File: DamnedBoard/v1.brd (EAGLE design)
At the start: 50.8 x 16.5 mm, 19 parts, among them J1 CORTEX_DEBUG_SMD, U1 EFM32ZG108, U2 MAX44009EDT+T21-0490D-M

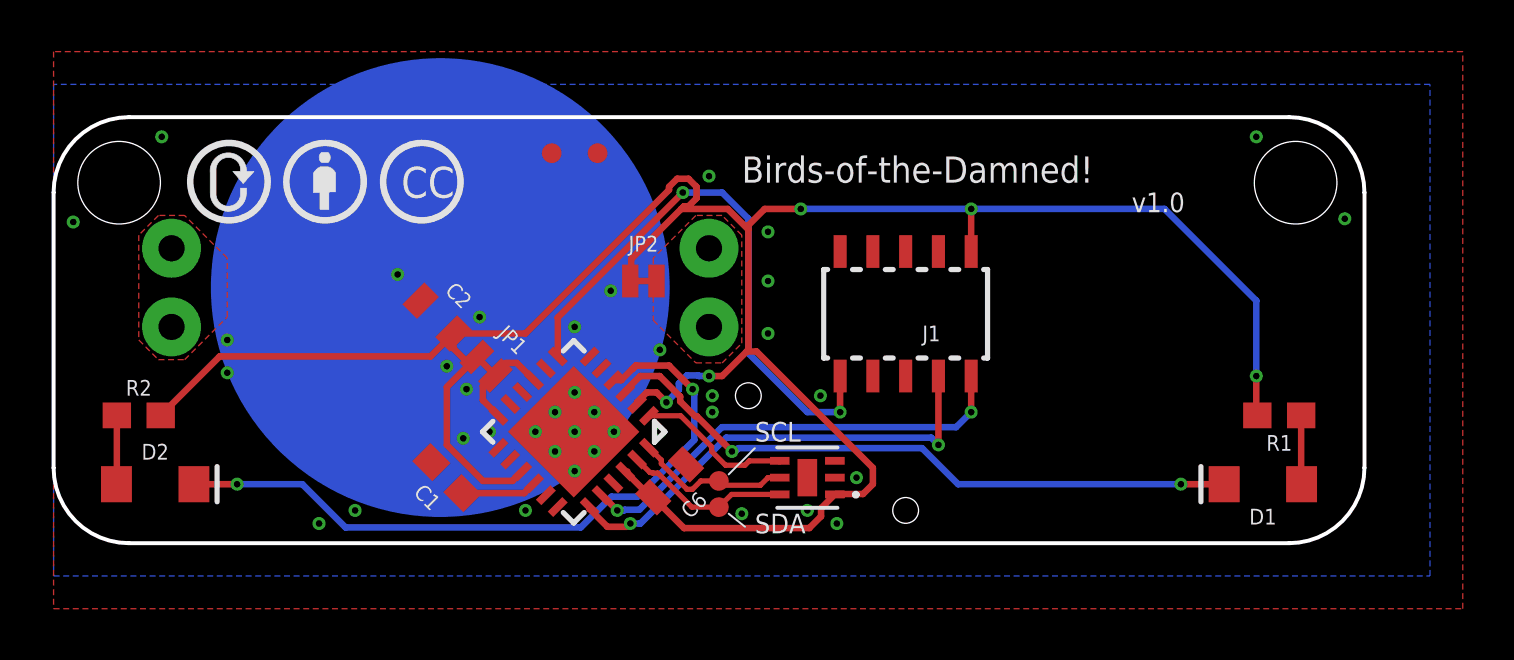
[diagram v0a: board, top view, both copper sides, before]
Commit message: Added pullups to i2c
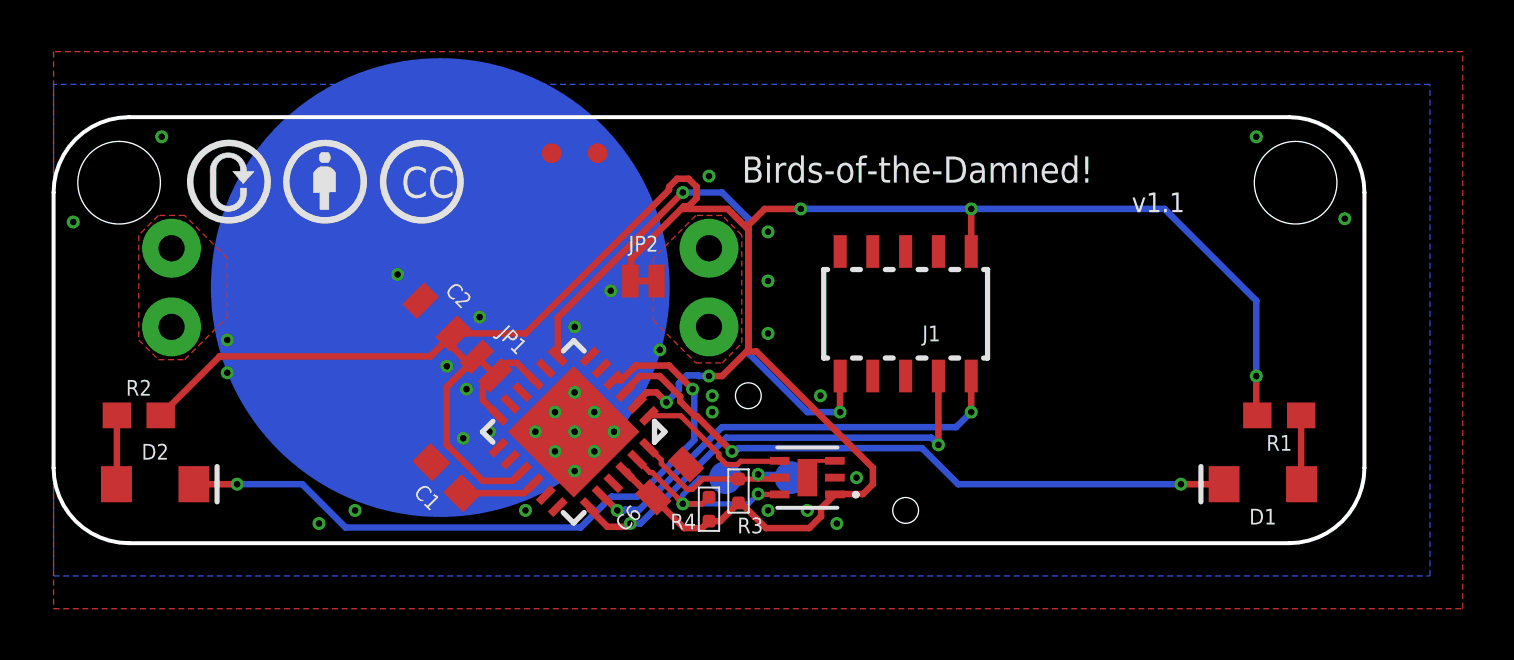
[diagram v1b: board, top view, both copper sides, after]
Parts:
- added R3, R4: 1K, Seeed-Resistor:R0402
- TP1, TP2: value TEST-POINT3 -> TEST-POINT3X5; device SparkFun-Connectors:PAD.03X.03 -> SparkFun-Connectors:PAD.03X.05
- moved TP2 2.80 mm to (28.6, 2.54), flipped to the bottom
- moved TP1 1.17 mm to (26.0, 2.54), flipped to the bottom
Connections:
- net SCL: now also R4.2
- net SDA: now also R3.1
- net VCC: now also R3.2, R4.1
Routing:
- net SDA: track 6.52 -> 9.84 mm, vias 0 -> 2
- net VSS: track 0.00 -> 1.63 mm
- net SCL: track 6.32 -> 7.51 mm, vias 0 -> 1
- net VCC: track 98.8 -> 99.6 mm
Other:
- board text added: "v1.1"
- board text removed: "v1.0"

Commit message: V1.1 pinout with all tests points.
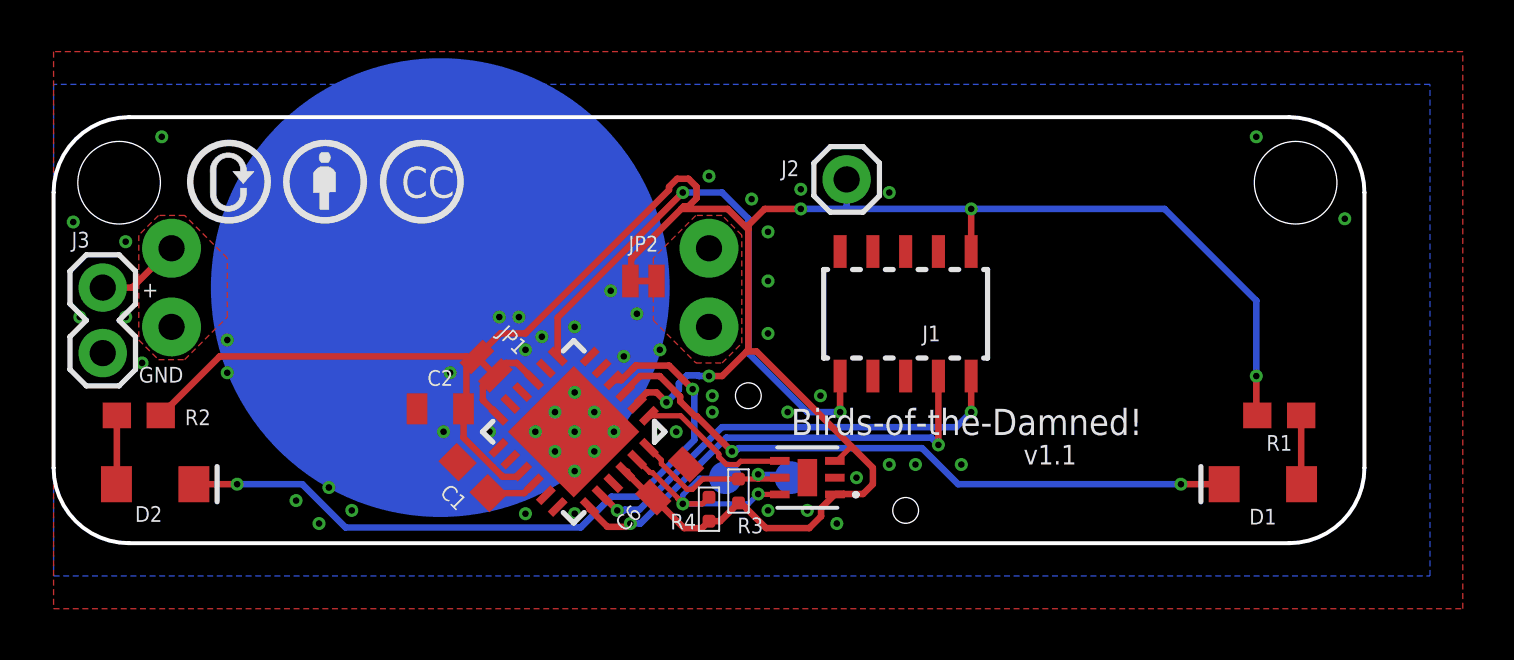
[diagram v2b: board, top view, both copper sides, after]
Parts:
- removed TP3, TP4: TEST-POINT3, SparkFun-Connectors:PAD.03X.03
- added J2: I_TEST, SparkFun-Connectors:1X01
- added J3: TEST, SparkFun-Connectors:1X02
- moved C2 3.56 mm to (15.0, 5.21), turned to 0 degrees
- moved C1 1.02 mm to (16.3, 2.54)
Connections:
- net +R: now also J3.2
- net VCC: now also J2.1, U2.3
- net VSS: now also J3.1; no longer TP3.P$1, TP4.P$1, U2.3
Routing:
- net +R: track 0.00 -> 3.30 mm
- net DCP: track 2.94 -> 1.92 mm
- net VSS: track 1.63 -> 0.71 mm, vias 39 -> 57
- net VCC: track 99.6 -> 98.9 mm
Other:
- board text added: "+"
- board text added: "GND"

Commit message: Progress on the adjustable version.
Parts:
- removed JP1: JUMPER-SMT_2_NC_TRACE_NO-SILK, SparkFun-Jumpers:SMT-JUMPER_2_NC_TRACE_NO-SILK
- added C3: 10nf, Seeed-Capacitor:C0402
- added R5: PV36W104C01B00, boneyard:POT_PV36W
- moved C2 2.47 mm to (16.4, 7.24), turned to 315 degrees
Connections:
- removed net AVDD: JP1.2, U1.12, U1.9
- removed net PA0: U1.1, U2.4
- removed net PC0: D1.C, U1.3
- removed net PC1: D2.C, U1.4
- new net ADJ: R5.2, U1.4
- new net EYE_L: D1.C, U1.1
- new net EYE_R: D2.C, U1.3
- new net WAKE: U1.21, U2.4
- net VCC: now also C3.2, R5.3, U1.12, U1.9; no longer JP1.1
- net VSS: now also C3.1, R5.1
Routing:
- net PC1: track 27.3 -> 0.00 mm, vias 2 -> 0
- net PC0: track 25.4 -> 0.00 mm, vias 2 -> 0
- net EYE_R: track 0.00 -> 23.5 mm, vias 0 -> 2
- net EYE_L: track 0.00 -> 19.7 mm, vias 0 -> 2
- net VCC: track 98.9 -> 85.7 mm, vias 5 -> 4
- net PA0: track 6.10 -> 0.00 mm
- net AVDD: track 4.09 -> 0.00 mm
- net VSS: vias 57 -> 51

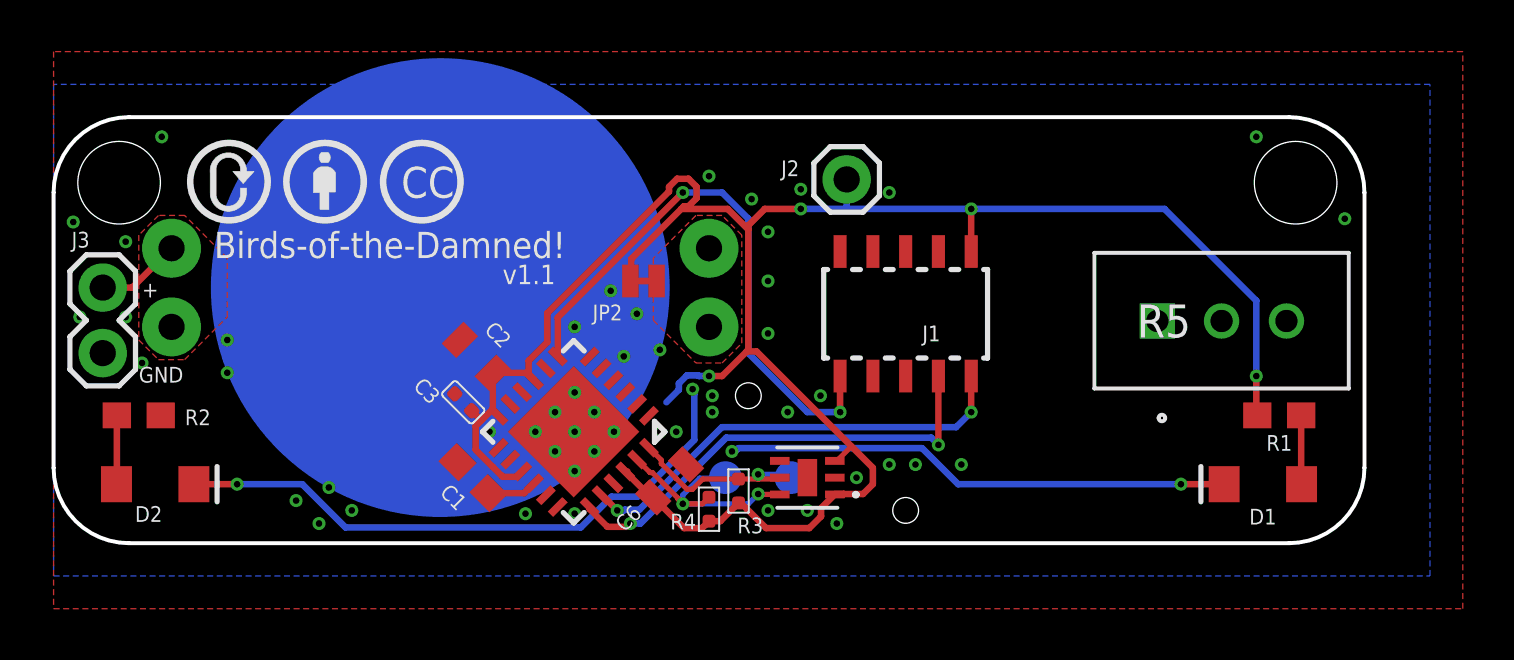
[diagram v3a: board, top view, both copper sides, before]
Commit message: Progress on v1.1
Added trim pot to use for light threshold adjustment.
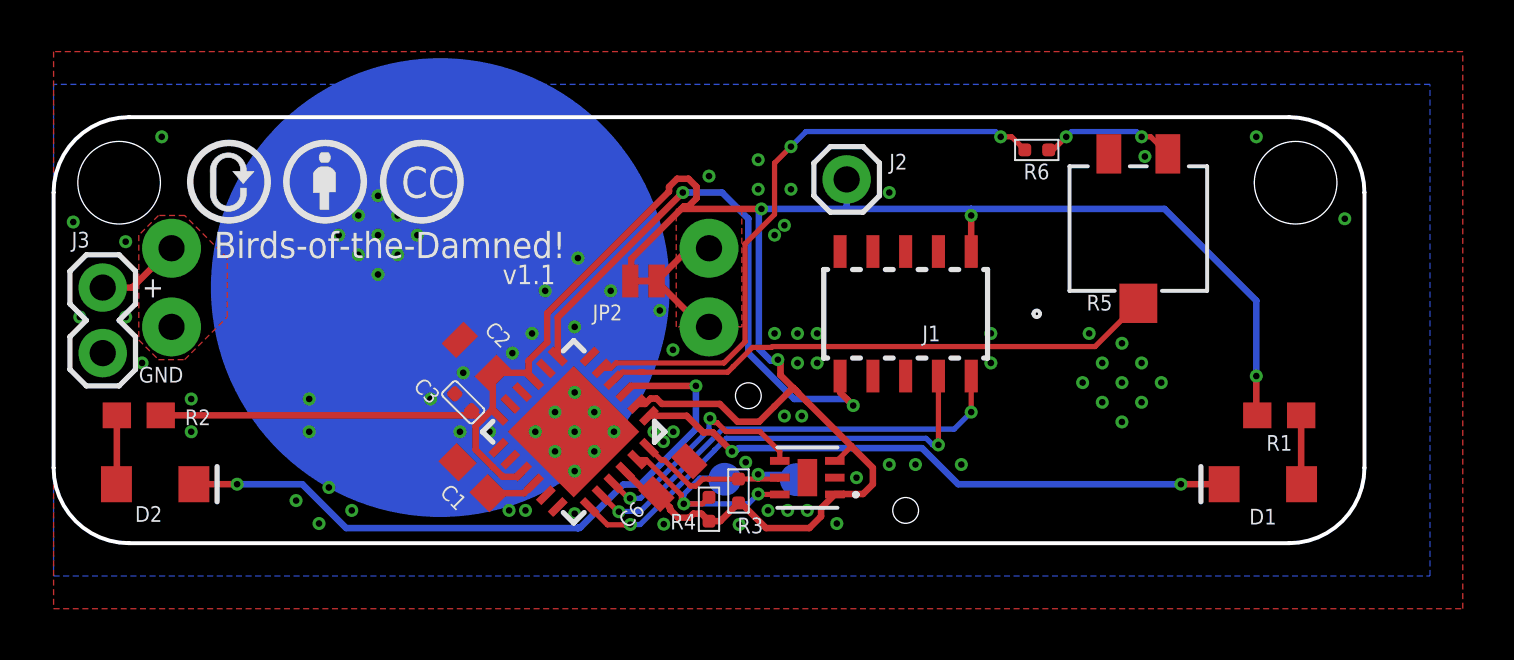
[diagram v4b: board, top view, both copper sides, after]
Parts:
- added R6: 1K, Seeed-Resistor:R0402
- R5: value PV36W104C01B00 -> 23BR100KLFTR; device boneyard:POT_PV36W -> boneyard:SOT_23BR100KLFTR
- moved R5 6.73 mm to (42.0, 12.2)
- moved TP2 0.22 mm to (28.8, 2.46)
- moved C6 0.18 mm to (24.0, 2.54)
- moved TP1 0.07 mm to (26.0, 2.48)
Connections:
- new net ADJ_PWR: R6.1, U1.5
- new net ADJ_PWR_SAFE: R5.3, R6.2
- net VCC: no longer R5.3
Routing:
- net ADJ_PWR: track 0.00 -> 23.9 mm, vias 0 -> 2
- net ADJ: track 0.00 -> 21.7 mm
- net VCC: track 85.7 -> 101.1 mm
- net WAKE: track 0.00 -> 9.10 mm, vias 0 -> 2
- net +L: track 0.00 -> 5.33 mm
- net ADJ_PWR_SAFE: track 0.00 -> 5.27 mm, vias 0 -> 2
- net EYE_L: track 19.7 -> 23.5 mm
- net EYE_R: track 23.5 -> 26.3 mm
- net VSS: vias 51 -> 90

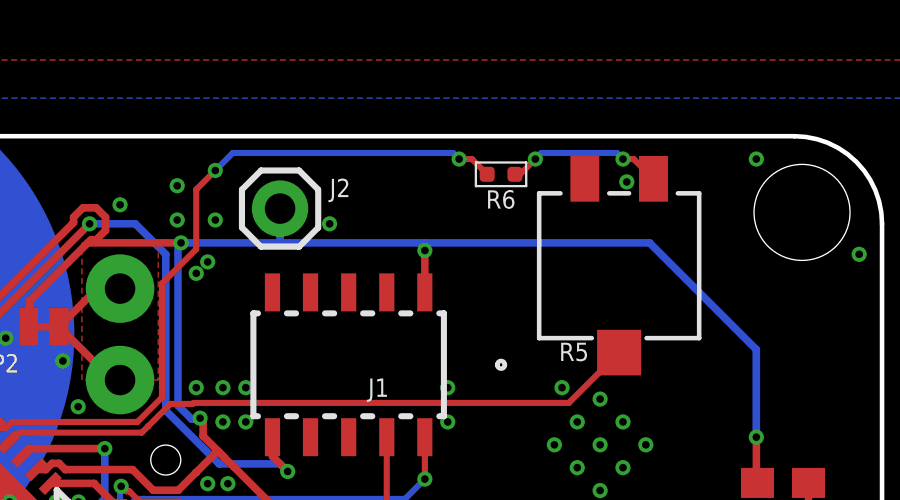
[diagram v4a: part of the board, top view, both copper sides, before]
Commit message: Adding Yakindu machine for firmware.
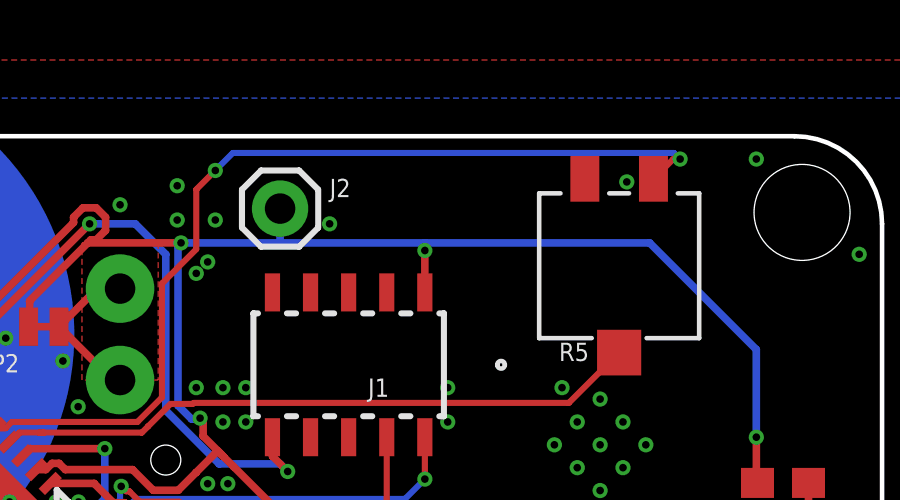
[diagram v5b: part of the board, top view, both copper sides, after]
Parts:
- removed R6: 1K, Seeed-Resistor:R0402
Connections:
- removed net ADJ_PWR_SAFE: R5.3, R6.2
- net ADJ_PWR: now also R5.3; no longer R6.1
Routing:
- net ADJ_PWR: track 23.9 -> 31.3 mm
- net ADJ_PWR_SAFE: track 5.27 -> 0.00 mm, vias 2 -> 0
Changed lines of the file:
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@@
 <layers>
 <layer number="1" name="Top" color="4" fill="1" visible="yes" active="yes"/>
-<layer number="16" name="Bottom" color="1" fill="1" visible="no" active="yes"/>
+<layer number="16" name="Bottom" color="1" fill="1" visible="yes" active="yes"/>
 <layer number="17" name="Pads" color="2" fill="1" visible="yes" active="yes"/>
 <layer number="18" name="Vias" color="2" fill="1" visible="yes" active="yes"/>
 <layer number="19" name="Unrouted" color="6" fill="1" visible="yes" active="yes"/>
 <layer number="20" name="Dimension" color="24" fill="1" visible="yes" active="yes"/>
-<layer number="21" name="tPlace" color="7" fill="1" visible="yes" active="yes"/>
-<layer number="22" name="bPlace" color="7" fill="1" visible="no" active="yes"/>
-<layer number="23" name="tOrigins" color="15" fill="1" visible="yes" active="yes"/>
-<layer number="24" name="bOrigins" color="15" fill="1" visible="no" active="yes"/>
-<layer number="25" name="tNames" color="7" fill="1" visible="yes" active="yes"/>
-<layer number="26" name="bNames" color="7" fill="1" visible="no" active="yes"/>
+<layer number="21" name="tPlace" color="7" fill="1" visible="no" active="yes"/>
+<layer number="22" name="bPlace" color="7" fill="1" visible="yes" active="yes"/>
+<layer number="23" name="tOrigins" color="15" fill="1" visible="no" active="yes"/>
+<layer number="24" name="bOrigins" color="15" fill="1" visible="yes" active="yes"/>
+<layer number="25" name="tNames" color="7" fill="1" visible="no" active="yes"/>
+<layer number="26" name="bNames" color="7" fill="1" visible="yes" active="yes"/>
 <layer number="27" name="tValues" color="7" fill="1" visible="no" active="yes"/>
 <layer number="28" name="bValues" color="7" fill="1" visible="no" active="yes"/>
@@
 <layer number="37" name="tTest" color="7" fill="1" visible="no" active="yes"/>
 <layer number="38" name="bTest" color="7" fill="1" visible="no" active="yes"/>
-<layer number="39" name="tKeepout" color="4" fill="11" visible="yes" active="yes"/>
-<layer number="40" name="bKeepout" color="1" fill="11" visible="no" active="yes"/>
-<layer number="41" name="tRestrict" color="4" fill="10" visible="yes" active="yes"/>
-<layer number="42" name="bRestrict" color="1" fill="10" visible="no" active="yes"/>
+<layer number="39" name="tKeepout" color="4" fill="11" visible="no" active="yes"/>
+<layer number="40" name="bKeepout" color="1" fill="11" visible="yes" active="yes"/>
+<layer number="41" name="tRestrict" color="4" fill="10" visible="no" active="yes"/>
+<layer number="42" name="bRestrict" color="1" fill="10" visible="yes" active="yes"/>
 <layer number="43" name="vRestrict" color="2" fill="10" visible="no" active="yes"/>
 <layer number="44" name="Drills" color="7" fill="1" visible="no" active="yes"/>
@@
 <layer number="49" name="Reference" color="7" fill="1" visible="no" active="yes"/>
 <layer number="50" name="dxf" color="7" fill="1" visible="no" active="no"/>
-<layer number="51" name="tDocu" color="7" fill="1" visible="yes" active="yes"/>
-<layer number="52" name="bDocu" color="7" fill="1" visible="no" active="yes"/>
+<layer number="51" name="tDocu" color="7" fill="1" visible="no" active="yes"/>
+<layer number="52" name="bDocu" color="7" fill="1" visible="yes" active="yes"/>
 <layer number="53" name="tGND_GNDA" color="7" fill="9" visible="no" active="no"/>
 <layer number="54" name="bGND_GNDA" color="1" fill="9" visible="no" active="no"/>
@@
 <attribute name="VALUE" x="13.809540625" y="5.371196875" size="0.635" layer="27" font="vector" ratio="10" rot="R315"/>
 </element>
-<element name="R6" library="Seeed-Resistor" library_urn="urn:adsk.eagle:library:474" package="R0402" package3d_urn="urn:adsk.eagle:package:32792/1" value="1K" x="38.1" y="15.24" smashed="yes" rot="R90">
-<attribute name="MPN" value="RC0402JR-071KL" x="38.1" y="15.24" size="1.778" layer="27" rot="R90" display="off"/>
-<attribute name="NAME" x="37.592" y="14.097" size="0.6096" layer="25" ratio="20"/>
-<attribute name="VALUE" x="36.83" y="13.716" size="0.889" layer="27" font="vector" ratio="11"/>
-</element>
 </elements>
 <signals>
@@
 <wire x1="26.797" y1="7.8033375" x2="26.797" y2="11.600575" width="0.2032" layer="1"/>
 <via x="28.575" y="15.367" extent="1-16" drill="0.254"/>
-<via x="36.703" y="15.748" extent="1-16" drill="0.254"/>
 <wire x1="27.94" y1="12.743575" x2="27.94" y2="14.732" width="0.2032" layer="1"/>
 <wire x1="27.94" y1="14.732" x2="28.575" y2="15.367" width="0.2032" layer="1"/>
-<wire x1="29.1592" y1="15.9512" x2="28.575" y2="15.367" width="0.2032" layer="16"/>
-<contactref element="R6" pad="1"/>
-<wire x1="37.6375" y1="15.24" x2="37.1295" y2="15.748" width="0.2032" layer="1"/>
-<wire x1="37.1295" y1="15.748" x2="36.703" y2="15.748" width="0.2032" layer="1"/>
-<wire x1="36.703" y1="15.748" x2="36.4998" y2="15.9512" width="0.2032" layer="16"/>
-<wire x1="36.4998" y1="15.9512" x2="29.1592" y2="15.9512" width="0.2032" layer="16"/>
-</signal>
-<signal name="ADJ_PWR_SAFE">
+<wire x1="28.575" y1="15.367" x2="29.1592" y2="15.9512" width="0.2032" layer="16"/>
 <contactref element="R5" pad="3"/>
-<contactref element="R6" pad="2"/>
-<via x="42.164" y="15.748" extent="1-16" drill="0.254"/>
-<via x="39.243" y="15.748" extent="1-16" drill="0.254"/>
-<wire x1="38.5625" y1="15.24" x2="38.735" y2="15.24" width="0.2032" layer="1"/>
-<wire x1="38.735" y1="15.24" x2="39.243" y2="15.748" width="0.2032" layer="1"/>
-<wire x1="42.164" y1="15.748" x2="42.5196" y2="15.748" width="0.2032" layer="1"/>
-<wire x1="42.5196" y1="15.748" x2="43.18" y2="15.0876" width="0.2032" layer="1"/>
-<wire x1="39.243" y1="15.748" x2="39.4462" y2="15.9512" width="0.2032" layer="16"/>
-<wire x1="41.9608" y1="15.9512" x2="42.164" y2="15.748" width="0.2032" layer="16"/>
-<wire x1="39.4462" y1="15.9512" x2="41.9608" y2="15.9512" width="0.2032" layer="16"/>
+<via x="44.069" y="15.748" extent="1-16" drill="0.254"/>
+<wire x1="43.8658" y1="15.9512" x2="44.069" y2="15.748" width="0.2032" layer="16"/>
+<wire x1="29.1592" y1="15.9512" x2="43.8658" y2="15.9512" width="0.2032" layer="16"/>
+<wire x1="44.069" y1="15.748" x2="43.8404" y2="15.748" width="0.2032" layer="1"/>
+<wire x1="43.8404" y1="15.748" x2="43.18" y2="15.0876" width="0.2032" layer="1"/>
 </signal>
 </signals>
